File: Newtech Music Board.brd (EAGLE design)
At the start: 133.3 x 79.7 mm, 56 parts, among them IC1 LM386N-1, J1 SS-30_BOARD_CONNECTOR, J2 MJ-3502N, U1 74LS10N, U2 74LS174N, U3 4050N, U4 4069N, U6 78L05

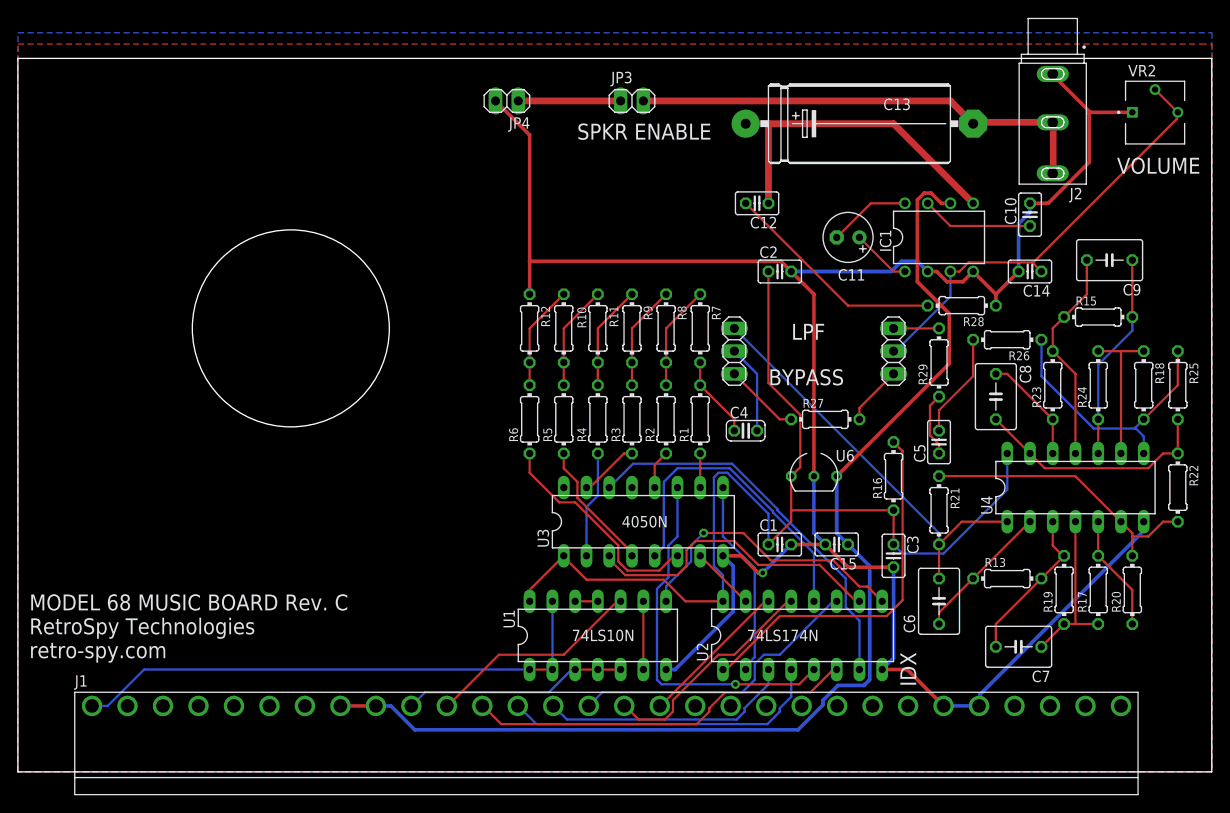
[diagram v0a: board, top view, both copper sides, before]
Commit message: Fixed the mixed up D7 and D5 lines
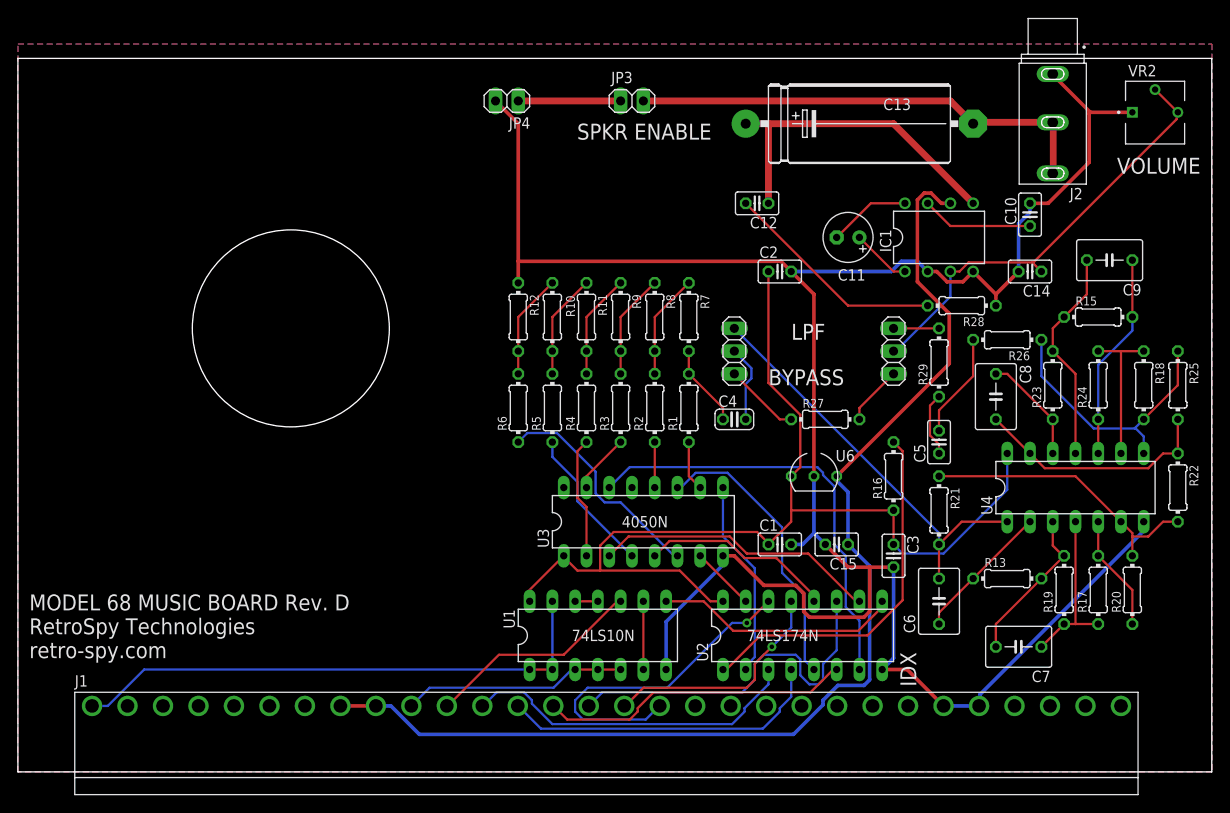
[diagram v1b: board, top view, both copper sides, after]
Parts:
- moved R5 1.80 mm to (59.7, 40.6)
- moved R1 1.80 mm to (74.9, 40.6)
- moved R11 1.80 mm to (59.7, 50.8)
- moved R2 1.80 mm to (71.1, 40.6)
- moved R3 1.80 mm to (67.3, 40.6)
- moved R4 1.80 mm to (63.5, 40.6)
- moved R6 1.80 mm to (55.9, 40.6)
- moved C4 1.80 mm to (80.0, 39.4)
- moved R10 1.80 mm to (63.5, 50.8)
- moved R12 1.80 mm to (55.9, 50.8)
- moved R7 1.80 mm to (74.9, 50.8)
- moved R8 1.80 mm to (71.1, 50.8)
- moved R9 1.80 mm to (67.3, 50.8)
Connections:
- net N$1: now also U2.3; no longer U2.6
- net N$3: now also U2.6; no longer U2.3
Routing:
- net N$8: track 17.0 -> 37.9 mm, vias 0 -> 1
- net N$13: track 35.4 -> 21.6 mm
- net GND: track 240.4 -> 253.5 mm, vias 1 -> 0
- net N$10: track 40.8 -> 32.2 mm, vias 1 -> 0
- net N$6: track 33.6 -> 41.6 mm
- net N$3: track 28.2 -> 34.8 mm
- net N$16: track 32.5 -> 27.2 mm, vias 1 -> 0
- net N$1: track 43.2 -> 38.0 mm
- net N$11: track 43.7 -> 48.7 mm
- net +5V: track 121.3 -> 118.3 mm
- net N$12: track 34.5 -> 31.8 mm
- net N$22: track 14.6 -> 16.4 mm
- net N$18: track 3.81 -> 5.61 mm
- net N$21: track 12.0 -> 13.5 mm
- net DAC_OUT: track 9.94 -> 8.67 mm
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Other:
- board text added: "MODEL 68 MUSIC BOARD Rev. D RetroSpy Technologies retro-spy.com"
- board text removed: "MODEL 68 MUSIC BOARD Rev. C RetroSpy Technologies retro-spy.com"
